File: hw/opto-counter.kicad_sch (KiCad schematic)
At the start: 13 parts, among them J1 IR-REC, J2 qwiic, J3 UPDI, U1 ATtiny1614-SS, U2 TSSP6038

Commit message: Remove gerbers and files that have been moved to `hw/`
Update .gitignore
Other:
- company: (none) -> Copyright 2023 Google LLC
- title: (none) -> Optical event counter
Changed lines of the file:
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@@
 (kicad_sch (version 20230121) (generator eeschema)
   (paper "A4")
+  (title_block
+    (title "Optical event counter")
+    (company "Copyright 2023 Google LLC")
+    (comment 2 "http://www.apache.org/licenses/LICENSE-2.0")
+    (comment 3 "Licensed under the Apache License, Version 2.0 (the \"License\").")
+  )
   (junction (at 157.48 41.91) (diameter 0) (color 0 0 0 0)
   )

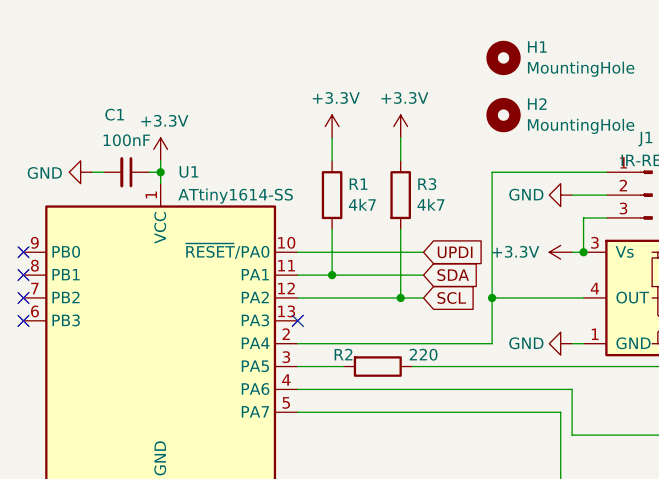
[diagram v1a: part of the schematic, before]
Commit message: Use ATtiny3224 as the mCPU in the schematic
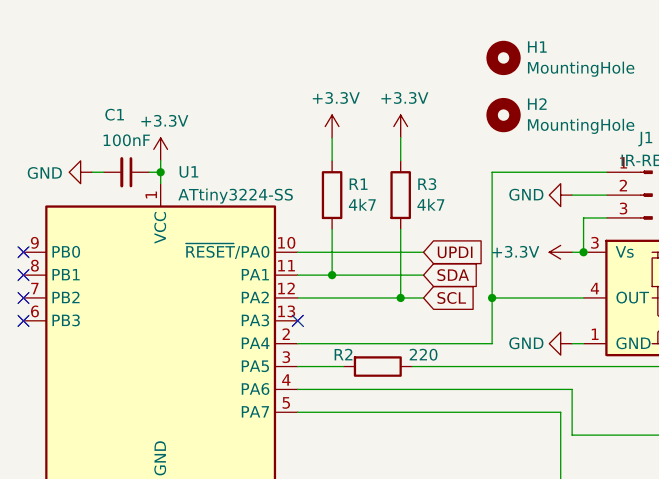
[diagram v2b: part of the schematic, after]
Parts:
- removed U1: ATtiny1614-SS, Package_SO:SOIC-14_3.9x8.7mm_P1.27mm, symbol MCU_Microchip_ATtiny:ATtiny1614-SS
- added U1: ATtiny3224-SS, Package_SO:SOIC-14_3.9x8.7mm_P1.27mm, symbol MCU_Microchip_ATtiny:ATtiny3224-SS
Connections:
- net +3V3: now also U1.1 (VCC)
- net GND: now also U1.14 (GND)
- net SCL: now also U1.12 (PA2)
- net SDA: now also U1.11 (PA1)
- net UPDI: now also U1.10 (~{RESET}/PA0)
- net at R2.2: now also U1.3 (PA5)
- net at J1.1 (Pin_1), U2.4 (OUT): now also U1.2 (PA4)
- net at D1.2 (A): now also U1.4 (PA6)
- net at D2.2 (A): now also U1.5 (PA7)
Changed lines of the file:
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@@
-    )
-  )
-  (symbol (lib_id "MCU_Microchip_ATtiny:ATtiny1614-SS") (at 110.49 52.07 0) (unit 1)
-    (in_bom yes) (on_board yes) (dnp no) (fields_autoplaced)
-    (property "Reference" "U1" (at 112.4459 33.02 0)
-      (effects (font (size 1.27 1.27)) (justify left))
-    )
-    (property "Value" "ATtiny1614-SS" (at 112.4459 35.56 0)
-      (effects (font (size 1.27 1.27)) (justify left))
-    )
-    (property "Footprint" "Package_SO:SOIC-14_3.9x8.7mm_P1.27mm" (at 110.49 52.07 0)
-      (effects (font (size 1.27 1.27) italic) hide)
-    )
-    (property "Datasheet" "http://ww1.microchip.com/downloads/en/DeviceDoc/ATtiny1614-data-sheet-40001995A.pdf" (at 110.49 52.07 0)
-      (effects (font (size 1.27 1.27)) hide)
-    )
-    (pin "1")
-    (pin "10")
-    (pin "11")
-    (pin "12")
-    (pin "13")
-    (pin "14")
-    (pin "2")
-    (pin "3")
-    (pin "4")
-    (pin "5")
-    (pin "6")
-    (pin "7")
-    (pin "8")
-    (pin "9")
-    (instances
-      (project "opto-counter"
-        (path "/ff1cffc4-9bfe-429d-a937-598850c99930"
-          (reference "U1") (unit 1)
-        )
-      )
     )
   )
@@
         )
       )
+    )
+  )
+  (symbol (lib_id "MCU_Microchip_ATtiny:ATtiny3224-SS") (at 110.49 52.07 0) (unit 1)
+    (in_bom yes) (on_board yes) (dnp no) (fields_autoplaced)
+    (property "Reference" "U1" (at 112.4459 33.02 0)
+      (effects (font (size 1.27 1.27)) (justify left))
+    )
+    (property "Value" "ATtiny3224-SS" (at 112.4459 35.56 0)
+      (effects (font (size 1.27 1.27)) (justify left))
+    )
+    (property "Footprint" "Package_SO:SOIC-14_3.9x8.7mm_P1.27mm" (at 110.49 52.07 0)
+      (effects (font (size 1.27 1.27) italic) hide)
+    )
+    (property "Datasheet" "https://ww1.microchip.com/downloads/en/DeviceDoc/ATtiny3224-3226-3227-Data-Sheet-DS40002345A.pdf" (at 110.49 52.07 0)
+      (effects (font (size 1.27 1.27)) hide)
+    )
+    (pin "1")
+    (pin "10")
+    (pin "11")
+    (pin "12")
+    (pin "13")
+    (pin "14")
+    (pin "2")
+    (pin "3")
+    (pin "4")
+    (pin "5")
+    (pin "6")
+    (pin "7")
+    (pin "8")
+    (pin "9")
+    (instances
+      (project "opto-counter"
+        (path "/ff1cffc4-9bfe-429d-a937-598850c99930"
+          (reference "U1") (unit 1)
+        )
+      )

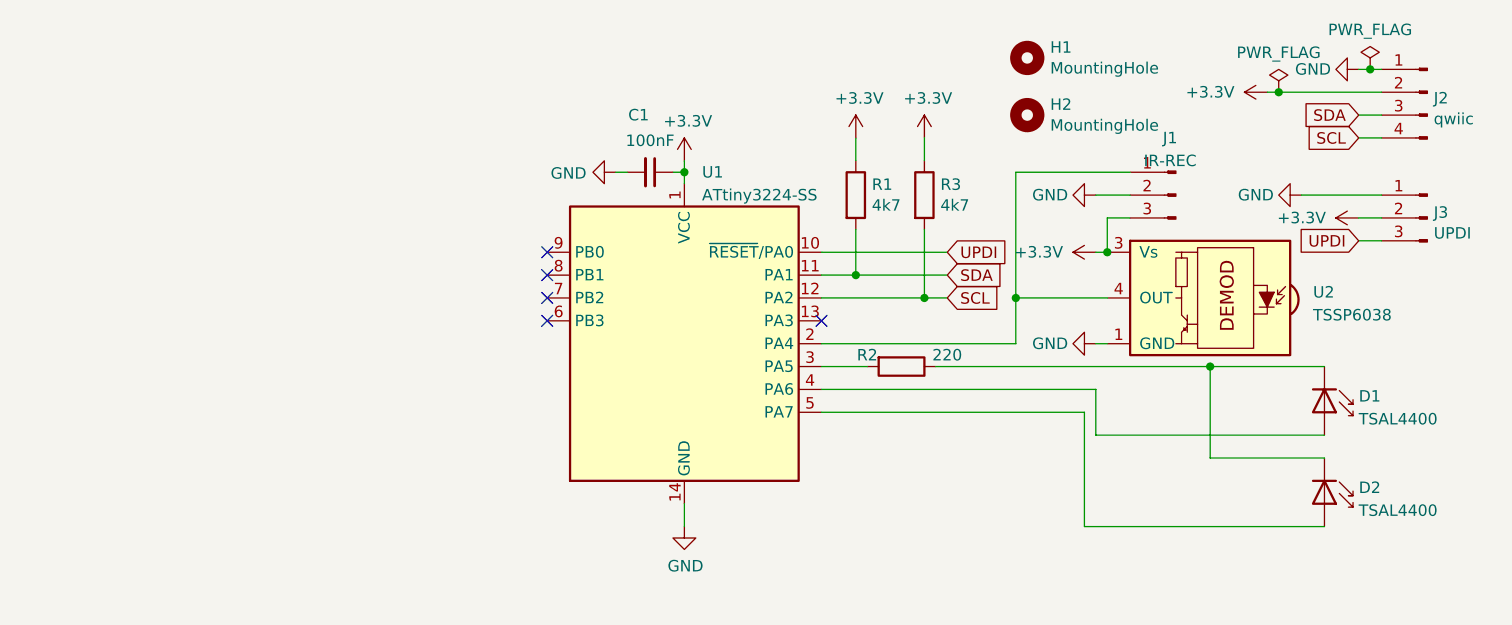
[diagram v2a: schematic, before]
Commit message: Fix the schematic to connect the led to the PB0 (WO0) PWM output of TCA
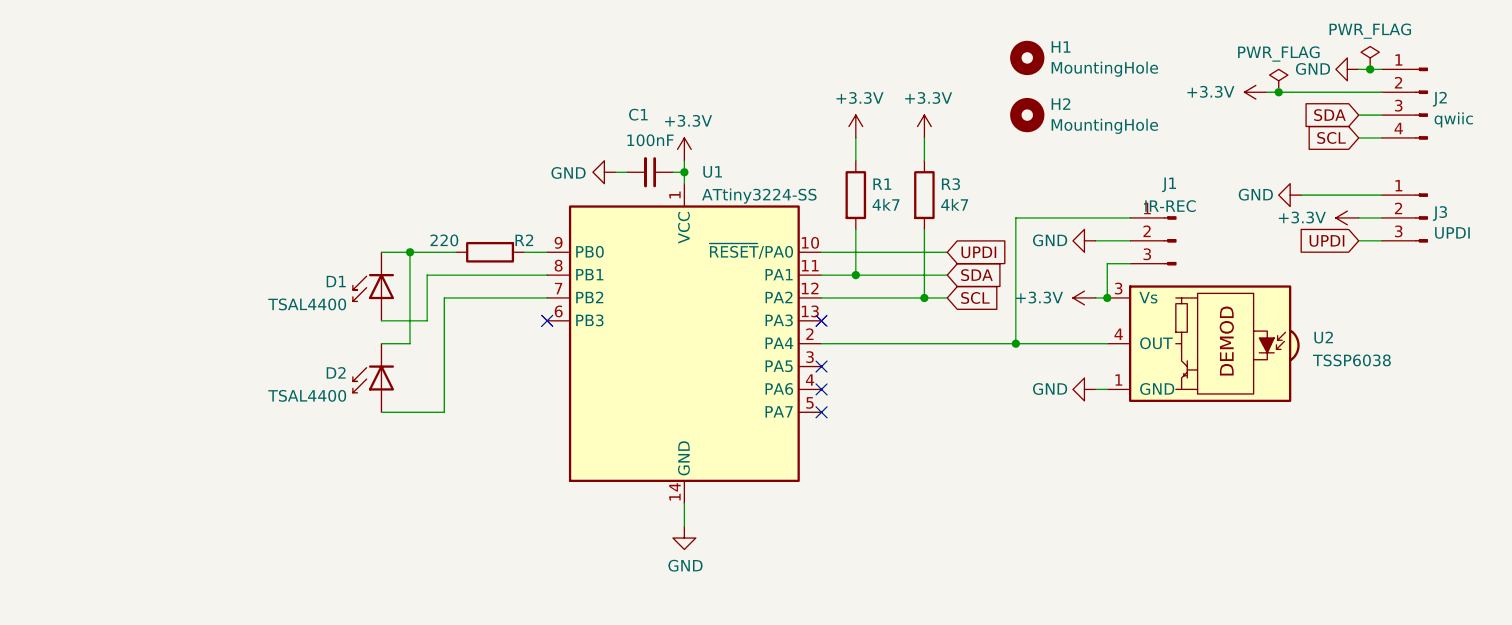
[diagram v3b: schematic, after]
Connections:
- net at R2.2: now also U1.9 (PB0); no longer U1.3 (PA5)
- net at D1.2 (A): now also U1.8 (PB1); no longer U1.4 (PA6)
- net at U1.5 (PA7): no longer D2.2 (A)
- net at U1.7 (PB2): now also D2.2 (A)
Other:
- moved on the sheet: D1, D2, J1, R2, U2

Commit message: Change the mCPU pins to match TWI
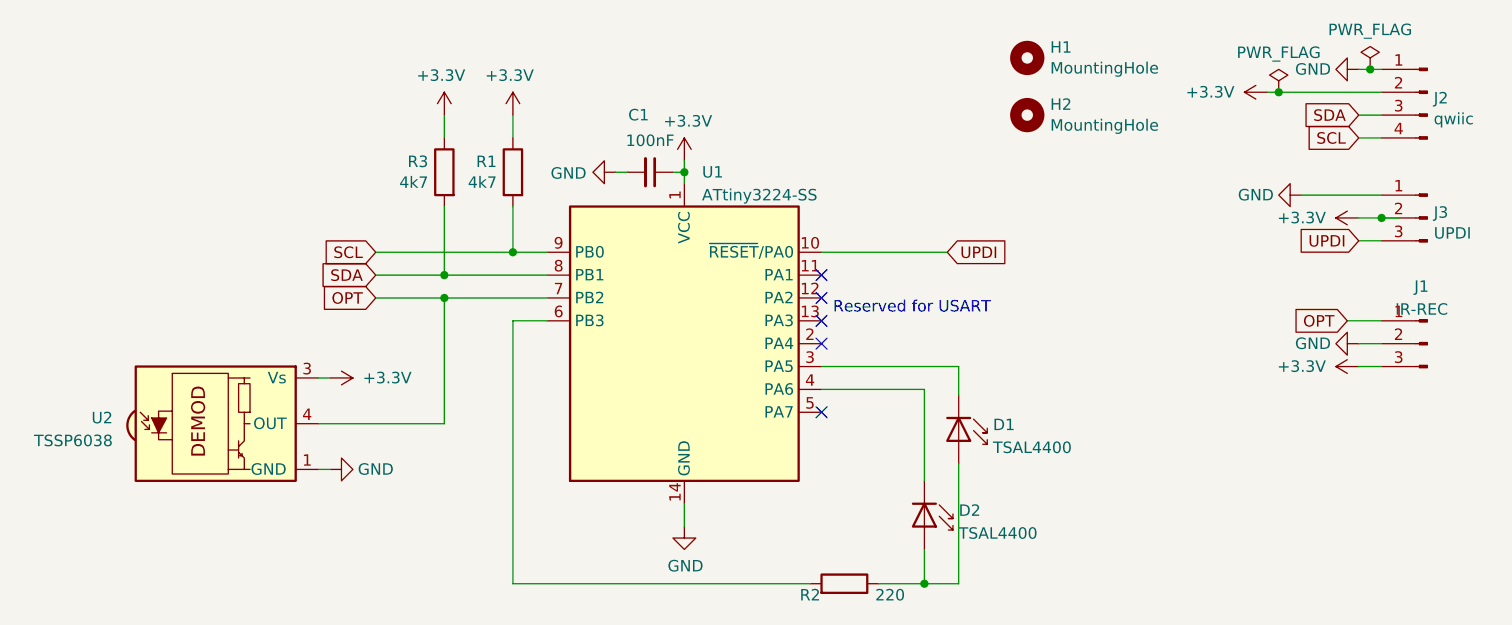
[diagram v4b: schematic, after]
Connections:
- net SCL: now also R1.2, U1.9 (PB0); no longer R3.2, U1.12 (PA2)
- net SDA: now also R3.2, U1.8 (PB1); no longer R1.2, U1.11 (PA1)
- net at R2.2: now also U1.6 (PB3); no longer U1.9 (PB0)
- net OPT: now reaches J1.1 (Pin_1), U2.4 (OUT)
- net OPT: now also U1.7 (PB2); no longer U1.2 (PA4)
- net at D1.2 (A): now also D2.2 (A), R2.1; no longer U1.8 (PB1)
- net at U1.3 (PA5): now also D1.1 (K)
- net at U1.4 (PA6): now also D2.1 (K)
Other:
- note added: "Reserved for USART"
- moved on the sheet: D1, D2, J1, R1, R2, R3, U2
